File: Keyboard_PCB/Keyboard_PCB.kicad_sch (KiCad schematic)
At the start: 42 parts, among them J1 JTAG, J3 LCD_MODULE, J4 FPC 30, J5 I2C_LCD, SW1 BTN, SW2 BTN, SW3 EC11E15244G1, U1 STM32F412CGUx, U7 W25Q128JVS, Y1 25MHz, Y2 32.768 KHz

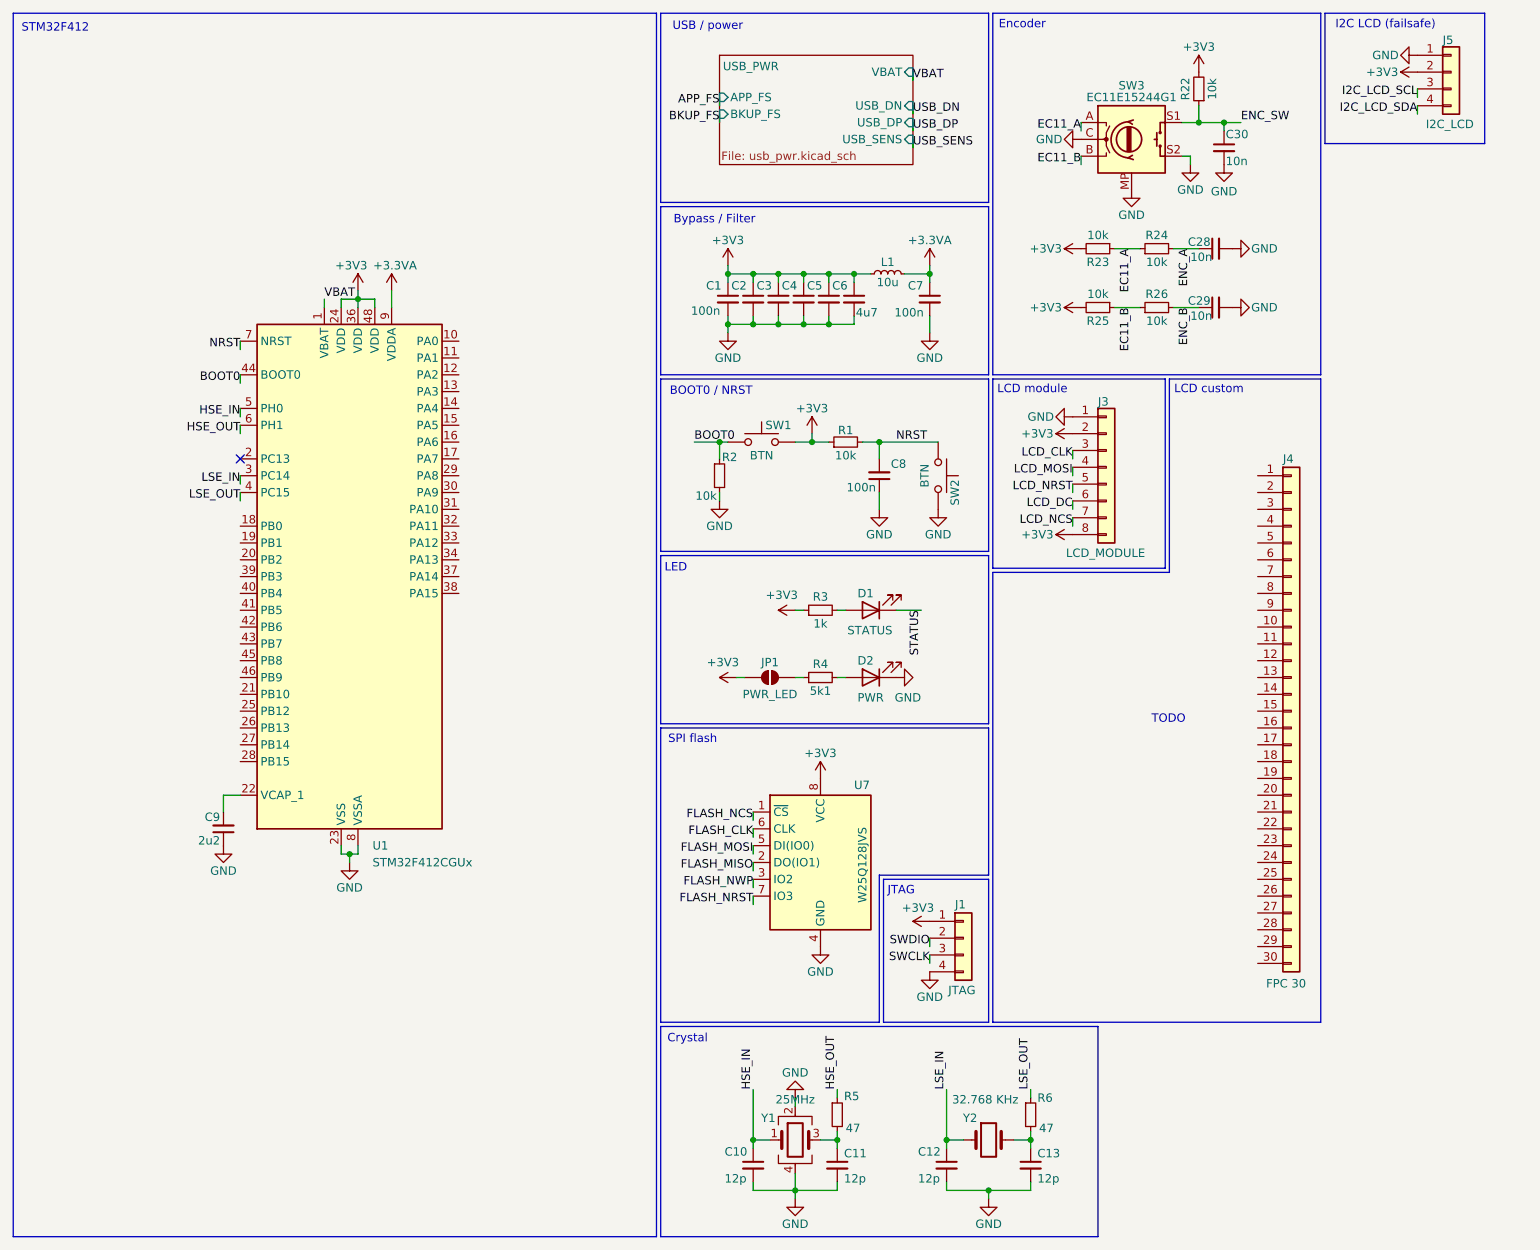
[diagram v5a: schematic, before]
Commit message: Footprint assignments
TODO: check FPC connector
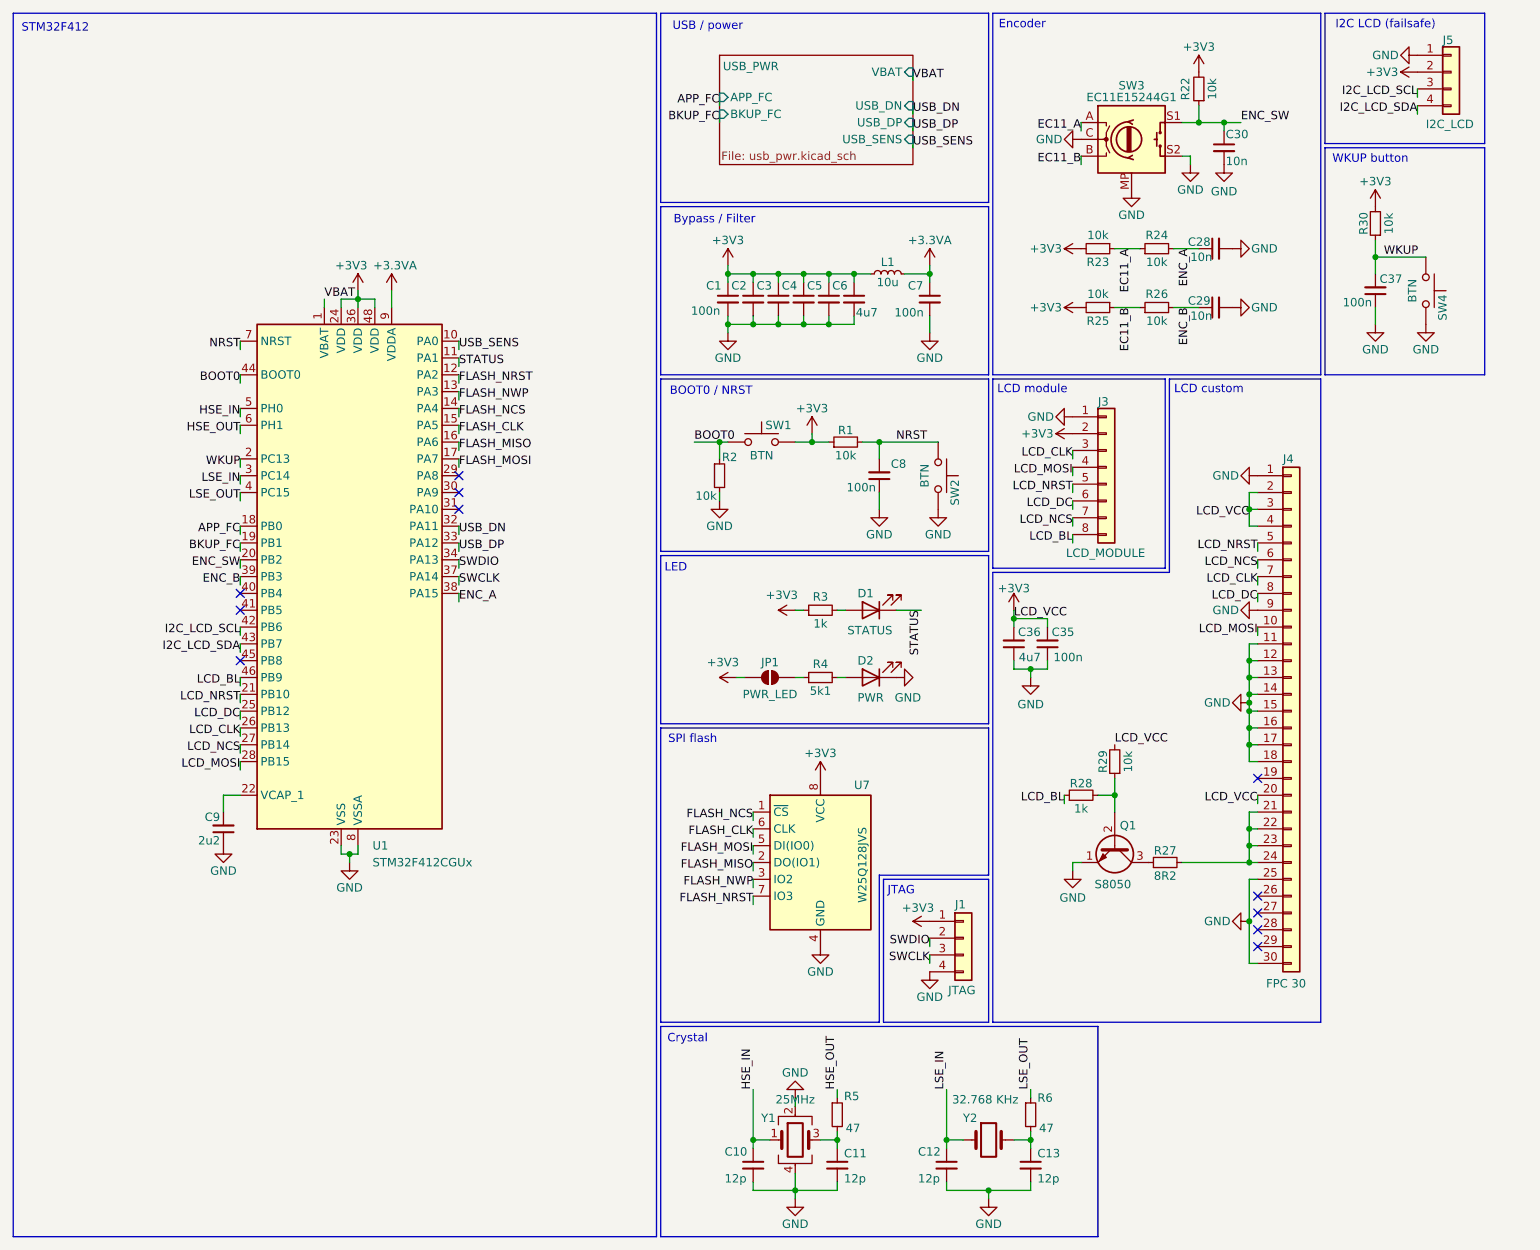
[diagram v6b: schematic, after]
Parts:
- added C35, C37: 100n, Capacitor_SMD:C_0603_1608Metric, symbol Device:C_Small
- added C36: 4u7, Capacitor_SMD:C_0603_1608Metric, symbol Device:C_Small
- added Q1: S8050, Package_TO_SOT_THT:TO-92_Inline, symbol Transistor_BJT:S8050
- added R27: 8R2, Resistor_SMD:R_0603_1608Metric, symbol Device:R_Small
- added R28: 1k, Resistor_SMD:R_0603_1608Metric, symbol Device:R_Small
- added R29, R30: 10k, Resistor_SMD:R_0603_1608Metric, symbol Device:R_Small
- added SW4: BTN, Button_Switch_SMD:SW_SPST_PTS810, symbol Switch:SW_Push
- J1: footprint Connector_PinHeader_2.00mm:PinHeader_1x04_P2.00mm_Vertical -> Connector_PinHeader_2.54mm:PinHeader_1x04_P2.54mm_Vertical
- J3: footprint (none) -> Connector_PinHeader_2.54mm:PinHeader_1x08_P2.54mm_Vertical
- J4: footprint (none) -> Connector_FFC-FPC:Hirose_FH12-30S-0.5SH_1x30-1MP_P0.50mm_Horizontal
- J5: footprint (none) -> Connector_PinHeader_2.54mm:PinHeader_1x04_P2.54mm_Vertical
- JP1: footprint (none) -> Jumper:SolderJumper-2_P1.3mm_Open_TrianglePad1.0x1.5mm
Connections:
- net +3V3: now also J4.2 (Pin_2), J4.20 (Pin_20), J4.3 (Pin_3), J4.4 (Pin_4), C35.2, C36.2, R29.2, R30.2; no longer J3.8 (Pin_8)
- net ENC_A: now also U1.38 (PA15)
- net ENC_B: now also U1.39 (PB3)
- net ENC_SW: now also U1.20 (PB2)
- net FLASH_CLK: now also U1.15 (PA5)
- net FLASH_MISO: now also U1.16 (PA6)
- net FLASH_MOSI: now also U1.17 (PA7)
- net FLASH_NCS: now also U1.14 (PA4)
- net FLASH_NRST: now also U1.12 (PA2)
- net FLASH_NWP: now also U1.13 (PA3)
- net GND: now also J4.1 (Pin_1), J4.11 (Pin_11), J4.12 (Pin_12), J4.13 (Pin_13), J4.14 (Pin_14), J4.15 (Pin_15), J4.16 (Pin_16), J4.17 (Pin_17), J4.18 (Pin_18), J4.25 (Pin_25), J4.30 (Pin_30), J4.9 (Pin_9), C35.1, C36.1, C37.1, Q1.1 (E), SW4.2
- net I2C_LCD_SCL: now also U1.42 (PB6)
- net I2C_LCD_SDA: now also U1.43 (PB7)
- net LCD_CLK: now also J4.7 (Pin_7), U1.26 (PB13)
- net LCD_DC: now also J4.8 (Pin_8), U1.25 (PB12)
- net LCD_MOSI: now also J4.10 (Pin_10), U1.28 (PB15)
- net LCD_NCS: now also J4.6 (Pin_6), U1.27 (PB14)
- net LCD_NRST: now also J4.5 (Pin_5), U1.21 (PB10)
- net STATUS: now also U1.11 (PA1)
- net SWCLK: now also U1.37 (PA14)
- net SWDIO: now also U1.34 (PA13)
- net USB_DN: now also U1.32 (PA11)
- net USB_DP: now also U1.33 (PA12)
- net USB_SENS: now also U1.10 (PA0)
- net APP_FC: now reaches U1.18 (PB0)
- net BKUP_FC: now reaches U1.19 (PB1)
- net WKUP: now reaches U1.2 (PC13)
- net WKUP: now also C37.2, R30.1, SW4.1
- net LCD_BL: now reaches U1.46 (PB9)
- net LCD_BL: now also J3.8 (Pin_8), R28.1
- net at J4.21 (Pin_21): now also J4.22 (Pin_22), J4.23 (Pin_23), J4.24 (Pin_24), R27.2
- new net: Q1.3 (C), R27.1
- new net: Q1.2 (B), R28.2, R29.1
- no-connect marks 1 -> 11
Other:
- sheet USB_PWR ports: added APP_FC, BKUP_FC; removed APP_FS, BKUP_FS
- note added: "WKUP button"
- note removed: "TODO"

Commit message: Layout progress
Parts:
- removed C2, C3: 100n, Capacitor_SMD:C_0603_1608Metric, symbol Device:C_Small
- J4: footprint Connector_FFC-FPC:Hirose_FH12-30S-0.5SH_1x30-1MP_P0.50mm_Horizontal -> Marijn_KiCad:SMD_FPC30
- renumbered C30 to C1, C8 to C10, C36 to C11, C35 to C12, C9 to C13, C28 to C2, C10 to C28, C11 to C29, C37 to C3, C12 to C30, C13 to C35, C1 to C4, C4 to C5, C5 to C6, C6 to C7, C7 to C8, C29 to C9, J5 to J1, J1 to J5, R22 to R1, R30 to R2, R1 to R22, R2 to R23, R3 to R24, R4 to R25, R29 to R26, R28 to R27, R27 to R28, R5 to R29, R23 to R3, R6 to R30, R24 to R4, R25 to R5, R26 to R6, SW3 to SW1, SW4 to SW2, SW1 to SW3, SW2 to SW4
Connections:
- net +3V3: no longer C4.1
- net VBAT: now also C4.1
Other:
- moved on the sheet: C4

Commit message: Battery charger layout done
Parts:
- removed Q1: S8050, Package_TO_SOT_THT:TO-92_Inline, symbol Transistor_BJT:S8050
- added Q1: S8050, Package_TO_SOT_SMD:SOT-23, symbol Marijn:S8050_SMD
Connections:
- net GND: now also Q1.2 (E)
- net at R28.1: now also Q1.3 (C)
- net at R26.1, R27.2: now also Q1.1 (B)
- net APP_FC: no longer names the net of U1.18 (PB0)
- net BKUP_FC: no longer names the net of U1.19 (PB1)
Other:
- sheet USB_PWR ports: added APP_CEN, APP_FC0, APP_FC1, BKUP_CEN, BKUP_FC0, BKUP_FC1; removed APP_FC, BKUP_FC
